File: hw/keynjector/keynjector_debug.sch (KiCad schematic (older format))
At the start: 1 part, among them J2 M50-3600542

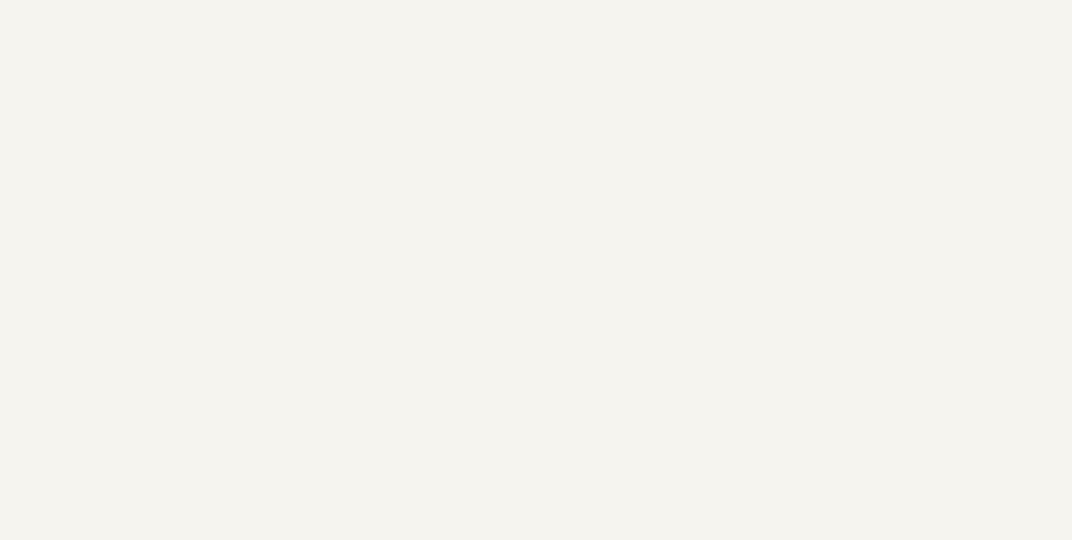
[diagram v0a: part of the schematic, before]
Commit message: added license text to KiCad sheets
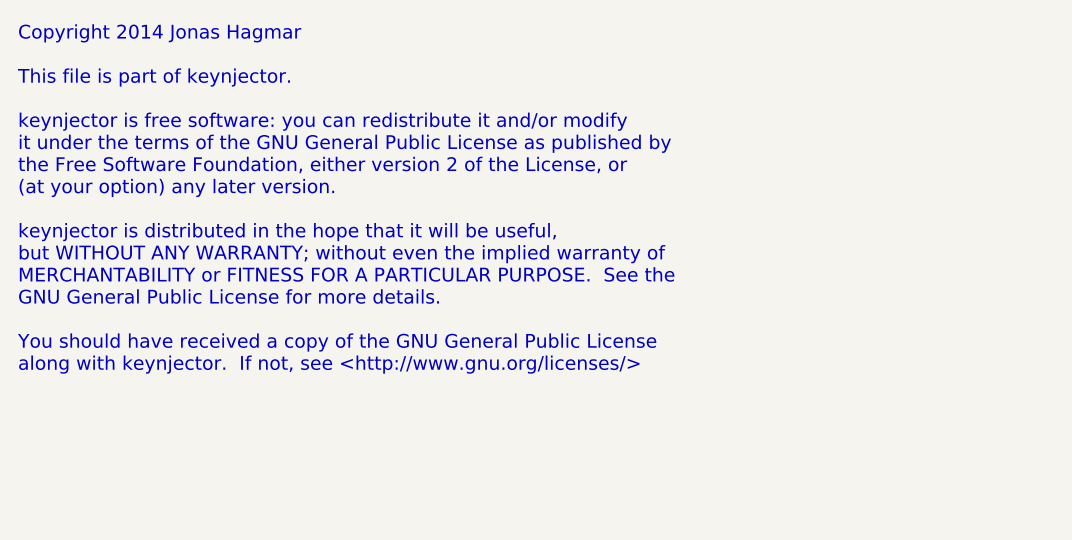
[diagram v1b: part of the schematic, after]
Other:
- note added: "Copyright 2014 Jonas Hagmar\n\nThis file is part of keynjector.\n\nkeynjector is free software: you can redistribute it and/or modify\nit under the terms of the GNU General Public License as published by\nthe Free Software Foundation, either version 2 of the License, or\n(at your option) any later version.\n\nkeynjector is distributed in the hope that it will be useful,\nbut WITHOUT ANY WARRANTY;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"
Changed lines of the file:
@@
 Sheet 5 7
 Title ""
-Date "6 nov 2014"
+Date "2 dec 2014"
 Rev ""
 Comp ""
@@
 Wire Wire Line
 	6550 3750 8100 3750
+Text Notes 800  850  0    60   ~ 0
+Copyright 2014 Jonas Hagmar\n\nThis file is part of keynjector.\n\nkeynjector is free software: you can redistribute it and/or modify\nit under the terms of the GNU General Public License as published by\nthe Free Software Foundation, either version 2 of the License, or\n(at your option) any later version.\n\nkeynjector is distributed in the hope that it will be useful,\nbut WITHOUT ANY WARRANTY; without even the implied warranty of\nMERCHANTABILITY or FITNESS FOR A PARTICULAR PURPOSE.  See the\nGNU General Public License for more details.\n\nYou should have received a copy of the GNU General Public License\nalong with keynjector.  If not, see <http://www.gnu.org/licenses/>
 $EndSCHEMATC
